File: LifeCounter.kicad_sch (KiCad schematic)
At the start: 0 parts

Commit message: added step-uop converter and inductor for backlight's LED power
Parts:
- added IC1: STM32H562RGT6, LifeCounter-Footprints:LQFP-64_10x10mm_P0.5mm_STM32, symbol LifeCounter-Symbols:STM32H562RGT6
- added J1: 54132-4562, LifeCounter-Footprints:Molex_54132-4562, symbol LifeCounter-Symbols:54132-4562
- added S1, S2, S3, S4, S5, S6, S7, S8: B3F-4050, LifeCounter-Footprints:Omron_B3F4050, symbol LifeCounter-Symbols:B3F-4050

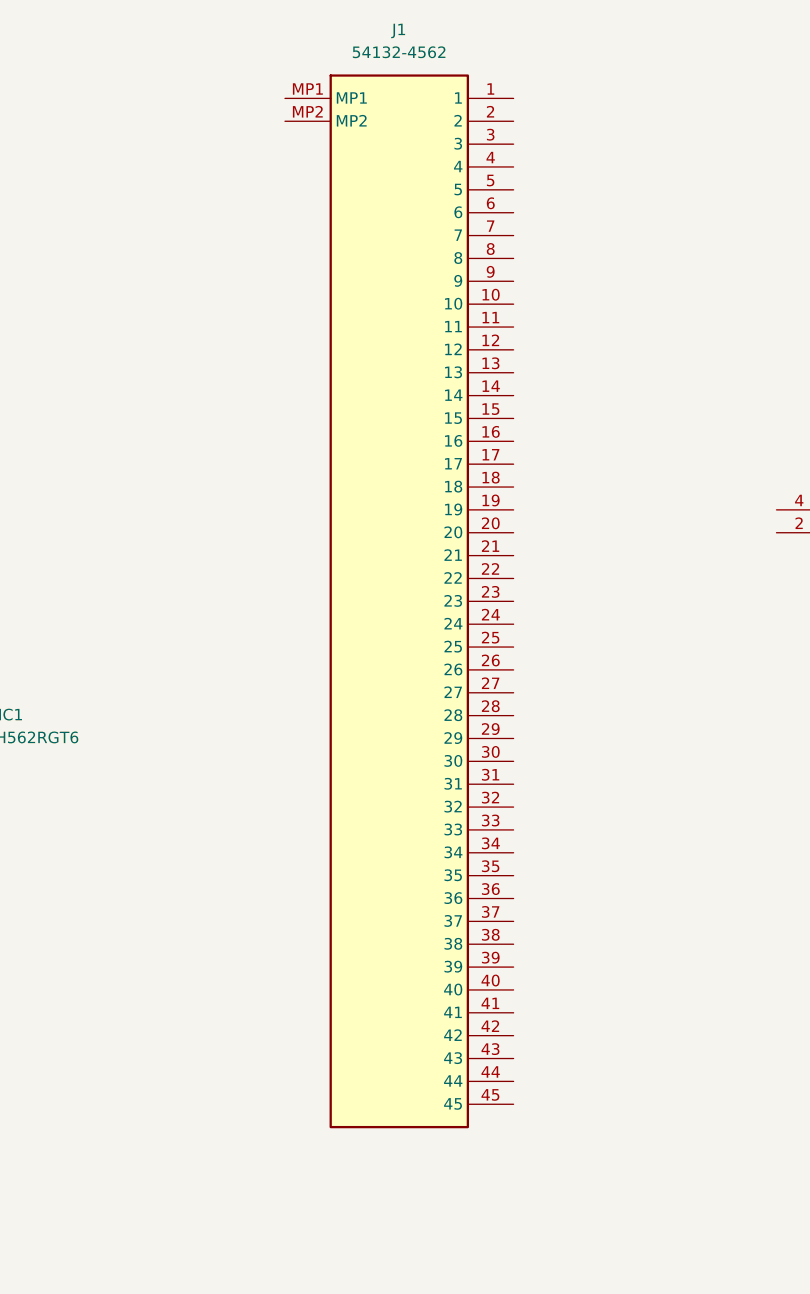
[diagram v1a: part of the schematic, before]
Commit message: imported the new footprints to footprints library
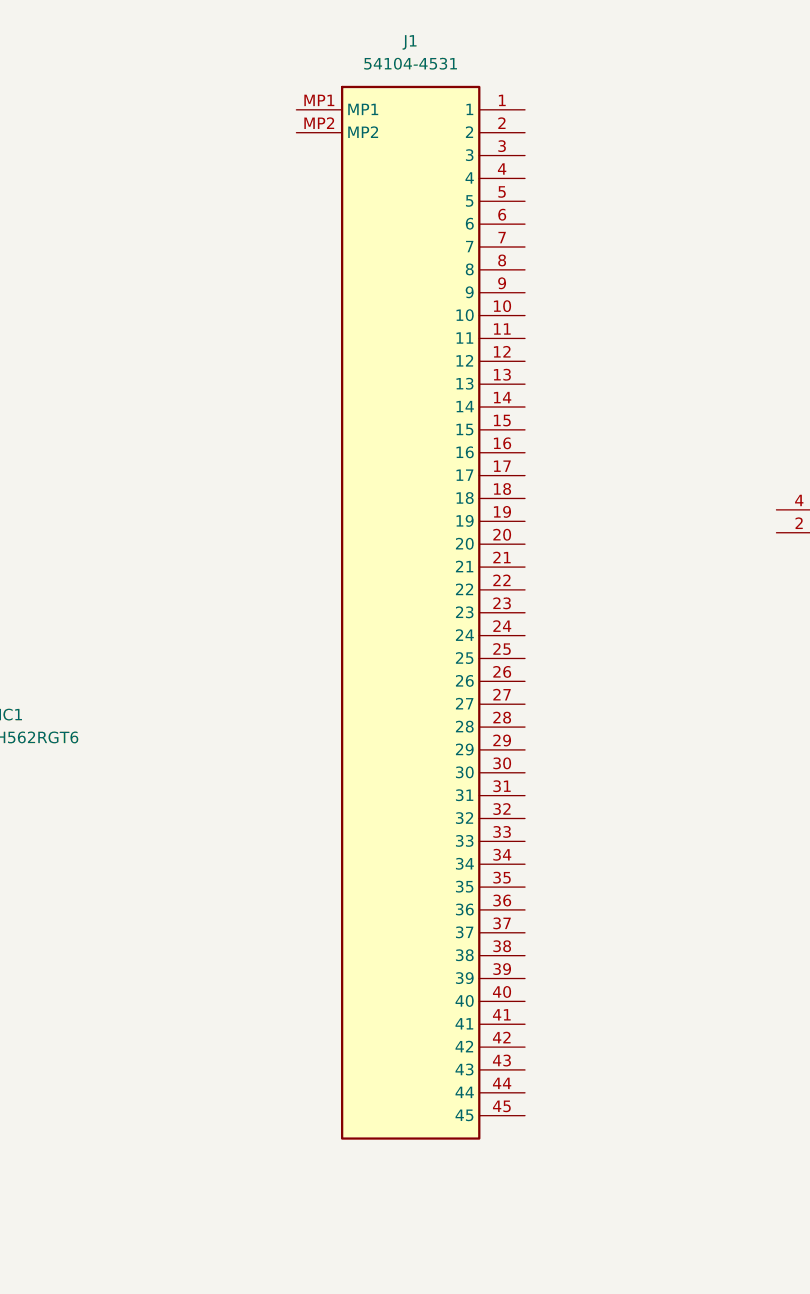
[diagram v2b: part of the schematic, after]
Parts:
- removed J1: 54132-4562, LifeCounter-Footprints:Molex_54132-4562, symbol LifeCounter-Symbols:54132-4562
- added J1: 54104-4531, LifeCounter-Footprints:Molex_54104-4531, symbol LifeCounter-Symbols:54104-4531
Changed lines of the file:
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@@
 	(paper "A4")
-	(symbol
-		(lib_id "LifeCounter-Symbols:54132-4562")
-		(at 127 36.83 0)
-		(unit 1)
-		(exclude_from_sim no)
-		(in_bom yes)
-		(on_board yes)
-		(dnp no)
-		(fields_autoplaced yes)
-		(property "Reference" "J1"
-			(at 139.7 29.21 0)
-			(effects
-				(font
-					(size 1.27 1.27)
-				)
-			)
-		)
-		(property "Value" "54132-4562"
-			(at 139.7 31.75 0)
-			(effects
-				(font
-					(size 1.27 1.27)
-				)
-			)
-		)
-		(property "Footprint" "LifeCounter-Footprints:Molex_54132-4562"
-			(at 148.59 131.75 0)
-			(effects
-				(font
-					(size 1.27 1.27)
-				)
-				(justify left top)
-				(hide yes)
-			)
-		)
-		(property "Datasheet" "https://www.molex.com/pdm_docs/sd/541324562_sd.pdf"
-			(at 148.59 231.75 0)
-			(effects
-				(font
-					(size 1.27 1.27)
-				)
-				(justify left top)
-				(hide yes)
-			)
-		)
-		(property "Description" "MOLEX - 54132-4562 - CONNECTOR, FPC, RECEPTACLE, 45 POSITION, 1ROW"
-			(at 127 36.83 0)
-			(effects
-				(font
-					(size 1.27 1.27)
-				)
-				(hide yes)
-			)
-		)
-		(property "Height" "2"
-			(at 148.59 431.75 0)
-			(effects
-				(font
-					(size 1.27 1.27)
-				)
-				(justify left top)
-				(hide yes)
-			)
-		)
-		(property "Mouser Part Number" "538-54132-4562"
-			(at 148.59 531.75 0)
-			(effects
-				(font
-					(size 1.27 1.27)
-				)
-				(justify left top)
-				(hide yes)
-			)
-		)
-		(property "Mouser Price/Stock" "https://www.mouser.co.uk/ProductDetail/Molex/54132-4562?qs=OdNwOVlk5%2FiIVqgFYVv71Q%3D%3D"
-			(at 148.59 631.75 0)
-			(effects
-				(font
-					(size 1.27 1.27)
-				)
-				(justify left top)
-				(hide yes)
-			)
-		)
-		(property "Manufacturer_Name" "Molex"
-			(at 148.59 731.75 0)
-			(effects
-				(font
-					(size 1.27 1.27)
-				)
-				(justify left top)
-				(hide yes)
-			)
-		)
-		(property "Manufacturer_Part_Number" "54132-4562"
-			(at 148.59 831.75 0)
-			(effects
-				(font
-					(size 1.27 1.27)
-				)
-				(justify left top)
-				(hide yes)
-			)
-		)
-		(pin "18"
-		)
-		(pin "8"
-		)
-		(pin "16"
-		)
-		(pin "14"
-		)
-		(pin "21"
-		)
-		(pin "23"
-		)
-		(pin "15"
-		)
-		(pin "22"
-		)
-		(pin "2"
-		)
-		(pin "1"
-		)
-		(pin "7"
-		)
-		(pin "20"
-		)
-		(pin "3"
-		)
-		(pin "17"
-		)
-		(pin "13"
-		)
-		(pin "4"
-		)
-		(pin "6"
-		)
-		(pin "40"
-		)
-		(pin "43"
-		)
-		(pin "11"
-		)
-		(pin "37"
-		)
-		(pin "38"
-		)
-		(pin "19"
-		)
-		(pin "30"
-		)
-		(pin "34"
-		)
-		(pin "29"
-		)
-		(pin "9"
-		)
-		(pin "31"
-		)
-		(pin "12"
-		)
-		(pin "45"
-		)
-		(pin "44"
-		)
-		(pin "5"
-		)
-		(pin "MP2"
-		)
-		(pin "26"
-		)
-		(pin "42"
-		)
-		(pin "36"
-		)
-		(pin "24"
-		)
-		(pin "25"
-		)
-		(pin "41"
-		)
-		(pin "28"
-		)
-		(pin "39"
-		)
-		(pin "27"
-		)
-		(pin "32"
-		)
-		(pin "33"
-		)
-		(pin "MP1"
-		)
-		(pin "35"
-		)
-		(pin "10"
-		)
-		(instances
-			(project ""
-				(path "/4fcff061-b5b1-4f40-9b81-6bf0aa8b3dad"
-					(reference "J1")
-					(unit 1)
-				)
-			)
-		)
-	)
 	(symbol
 		(lib_id "LifeCounter-Symbols:B3F-4050")
@@
 					(unit 1)
 				)
+			)
+		)
+	)
+	(symbol
+		(lib_id "LifeCounter-Symbols:54104-4531")
+		(at 128.27 38.1 0)
+		(unit 1)
+		(exclude_from_sim no)
+		(in_bom yes)
+		(on_board yes)
+		(dnp no)
+		(fields_autoplaced yes)
+		(property "Reference" "J1"
+			(at 140.97 30.48 0)
+			(effects
+				(font
+					(size 1.27 1.27)
+				)
+			)
+		)
+		(property "Value" "54104-4531"
+			(at 140.97 33.02 0)
+			(effects
+				(font
+					(size 1.27 1.27)
+				)
+			)
+		)
+		(property "Footprint" "LifeCounter-Footprints:Molex_54104-4531"
+			(at 149.86 133.02 0)
+			(effects
+				(font
+					(size 1.27 1.27)
+				)
+				(justify left top)
+				(hide yes)
+			)
+		)
+		(property "Datasheet" ""
+			(at 149.86 233.02 0)
+			(effects
+				(font
+					(size 1.27 1.27)
+				)
+				(justify left top)
+				(hide yes)
+			)
+		)
+		(property "Description" "FFC & FPC Connectors 0.5 FPC ZIF SMT R/AU prCont45CktEmbsTpPkg"
+			(at 128.27 38.1 0)
+			(effects
+				(font
+					(size 1.27 1.27)
+				)
+				(hide yes)
+			)
+		)
+		(property "Height" "2"
+			(at 149.86 433.02 0)
+			(effects
+				(font
+					(size 1.27 1.27)
+				)
+				(justify left top)
+				(hide yes)
+			)
+		)
+		(property "Mouser Part Number" "538-54104-4531"
+			(at 149.86 533.02 0)
+			(effects
+				(font
+					(size 1.27 1.27)
+				)
+				(justify left top)
+				(hide yes)
+			)
+		)
+		(property "Mouser Price/Stock" "https://www.mouser.co.uk/ProductDetail/Molex/54104-4531?qs=sMDukONGwJXyyUSAdQyS2w%3D%3D"
+			(at 149.86 633.02 0)
+			(effects
+				(font
+					(size 1.27 1.27)
+				)
+				(justify left top)
+				(hide yes)
+			)
+		)
+		(property "Manufacturer_Name" "Molex"
+			(at 149.86 733.02 0)
+			(effects
+				(font
+					(size 1.27 1.27)
+				)
+				(justify left top)
+				(hide yes)
+			)
+		)
+		(property "Manufacturer_Part_Number" "54104-4531"
+			(at 149.86 833.02 0)
+			(effects
+				(font
+					(size 1.27 1.27)
+				)
+				(justify left top)
+				(hide yes)
+			)
+		)
+		(pin "39"
+		)
+		(pin "19"
+		)
+		(pin "40"
+		)
+		(pin "31"
+		)
+		(pin "23"
+		)
+		(pin "29"
+		)
+		(pin "8"
+		)
+		(pin "11"
+		)
+		(pin "5"
+		)
+		(pin "4"
+		)
+		(pin "3"
+		)
+		(pin "2"
+		)
+		(pin "1"
+		)
+		(pin "MP2"
+		)
+		(pin "MP1"
+		)
+		(pin "20"
+		)
+		(pin "41"
+		)
+		(pin "33"
+		)
+		(pin "16"
+		)
+		(pin "43"
+		)
+		(pin "32"
+		)
+		(pin "18"
+		)
+		(pin "28"
+		)
+		(pin "45"
+		)
+		(pin "44"
+		)
+		(pin "25"
+		)
+		(pin "37"
+		)
+		(pin "38"
+		)
+		(pin "9"
+		)
+		(pin "13"
+		)
+		(pin "21"
+		)
+		(pin "34"
+		)
+		(pin "36"
+		)
+		(pin "14"
+		)
+		(pin "17"
+		)
+		(pin "42"
+		)
+		(pin "26"
+		)
+		(pin "7"
+		)
+		(pin "35"
+		)
+		(pin "22"
+		)
+		(pin "15"
+		)
+		(pin "10"
+		)
+		(pin "6"
+		)
+		(pin "12"
+		)
+		(pin "24"
+		)
+		(pin "27"
+		)
+		(pin "30"
+		)
+		(instances
+			(project ""
+				(path "/4fcff061-b5b1-4f40-9b81-6bf0aa8b3dad"
+					(reference "J1")
+					(unit 1)
+				)

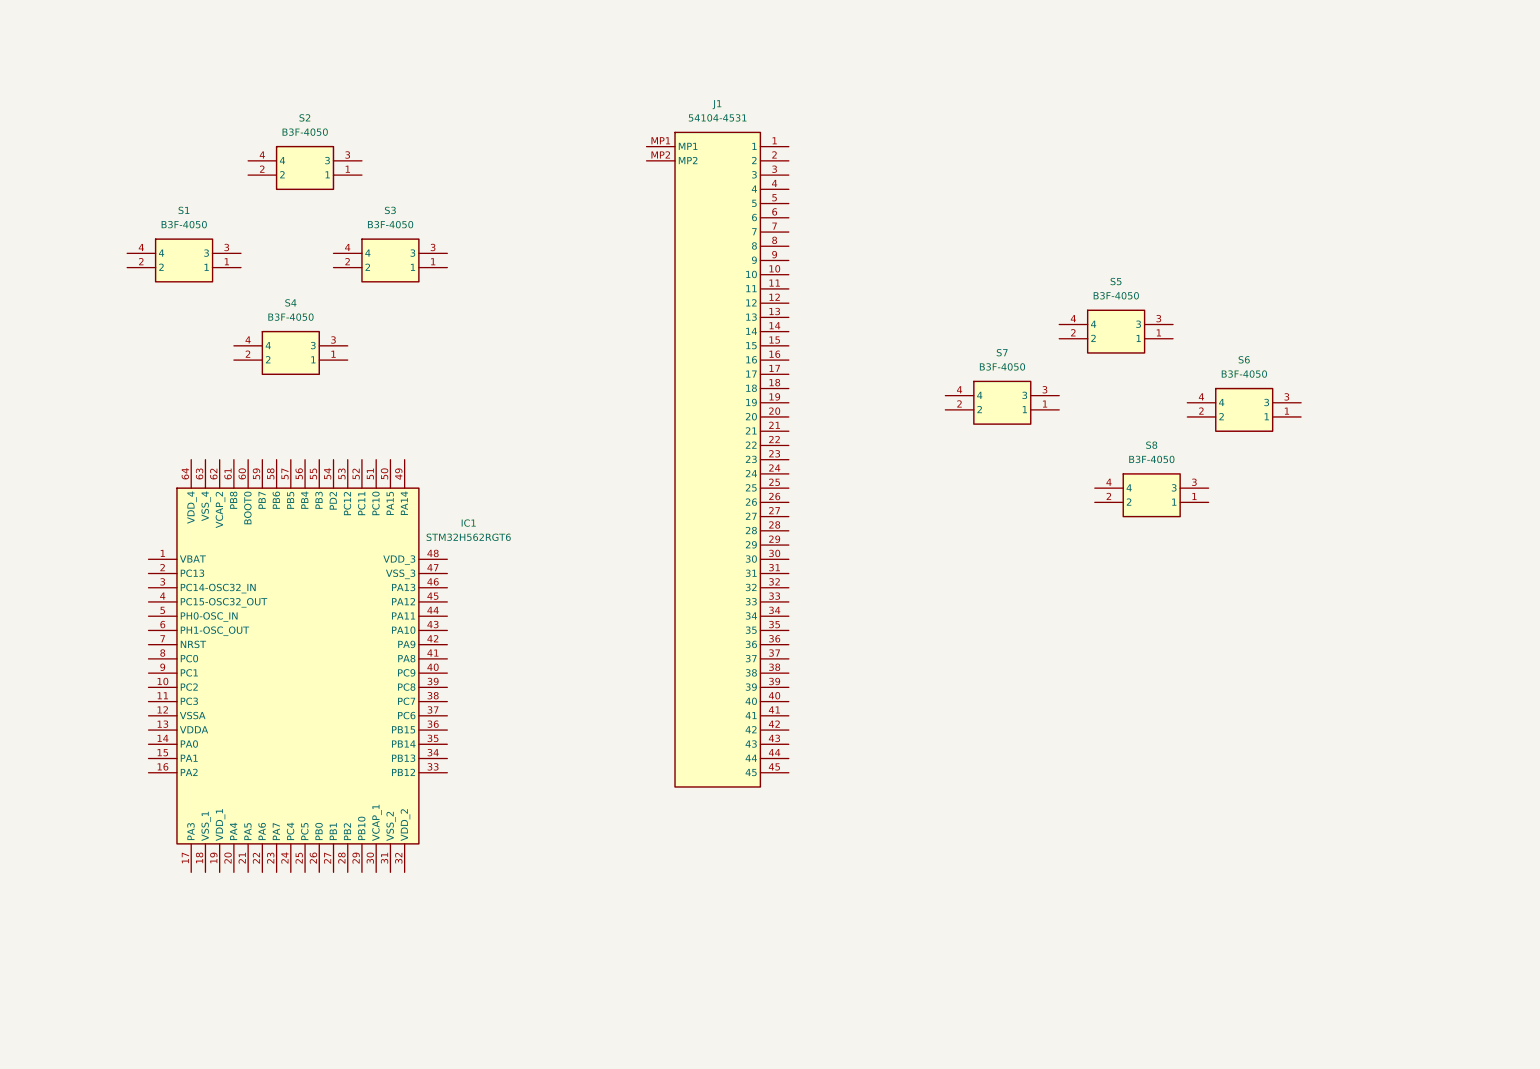
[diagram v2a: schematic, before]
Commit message: finished the power circuit for the LCD backlight
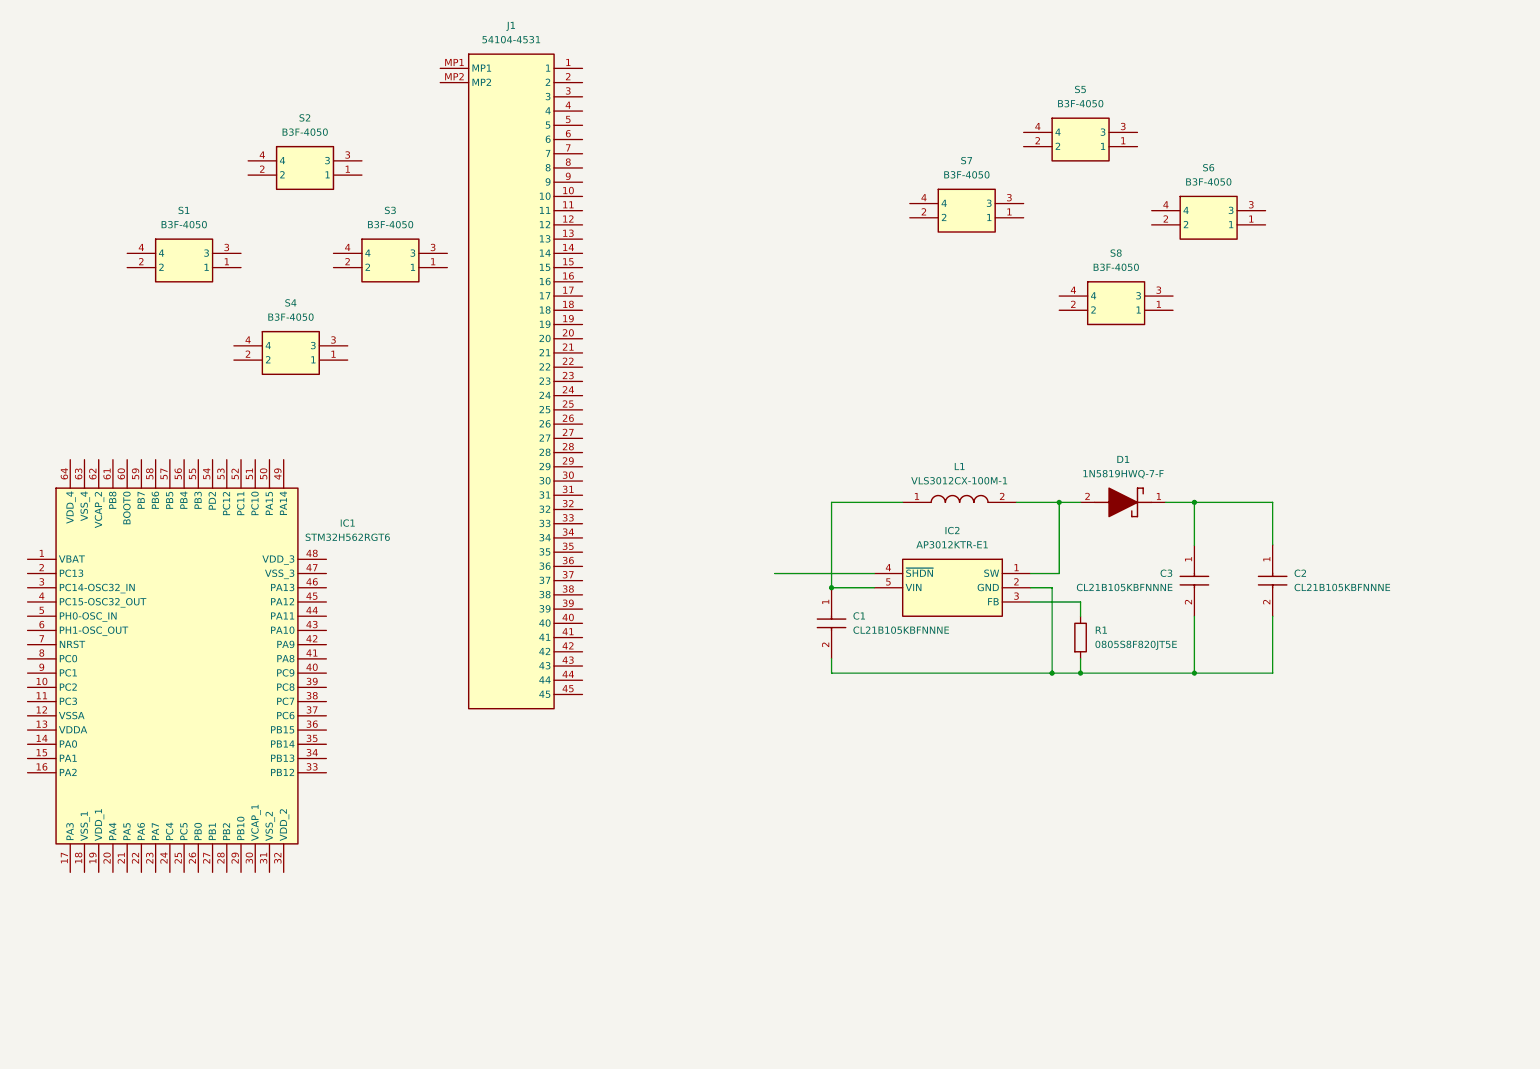
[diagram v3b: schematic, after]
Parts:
- added C1, C2, C3: CL21B105KBFNNNE, LifeCounter-Footprints:Samsung_CAPC2012X135M, symbol LifeCounter-Symbols:CL21B105KBFNNNE
- added D1: 1N5819HWQ-7-F, LifeCounter-Footprints:Diodes-Inc_SOD3716X145M, symbol LifeCounter-Symbols:1N5819HWQ-7-F
- added IC2: AP3012KTR-E1, LifeCounter-Footprints:Diodes-Inc_SOT95P282X145-5M, symbol LifeCounter-Symbols:AP3012KTR-E1
- added L1: VLS3012CX-100M-1, LifeCounter-Footprints:TDK_VLS3012, symbol LifeCounter-Symbols:VLS3012CX-100M-1
- added R1: 0805S8F820JT5E, Resistor_SMD:R_0805_2012Metric_Pad1.20x1.40mm_HandSolder, symbol Device:R
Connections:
- new net: C2.1, C3.1, D1.1 (K)
- new net: C1.2, C2.2, C3.2, IC2.2 (GND), R1.2
- new net: IC2.3 (FB), R1.1
- new net: D1.2 (A), IC2.1 (SW), L1.2
- new net: C1.1, IC2.5 (VIN), L1.1
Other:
- moved on the sheet: IC1, J1, S5, S6, S7, S8
